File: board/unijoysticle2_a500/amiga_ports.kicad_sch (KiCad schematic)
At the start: 23 parts, among them J2 PORT JOY #1, J3 PORT JOY #2, SW3 MOUSE, SW4 SWAP, U4 74HC05, U5 74HC05, U6 74HC05

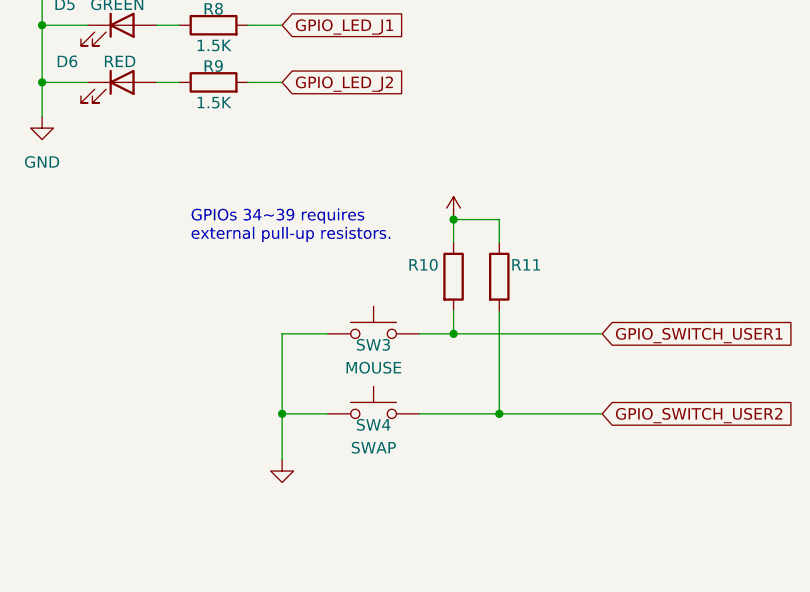
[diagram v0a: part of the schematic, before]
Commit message: a500: layout with open hardware logo in copper
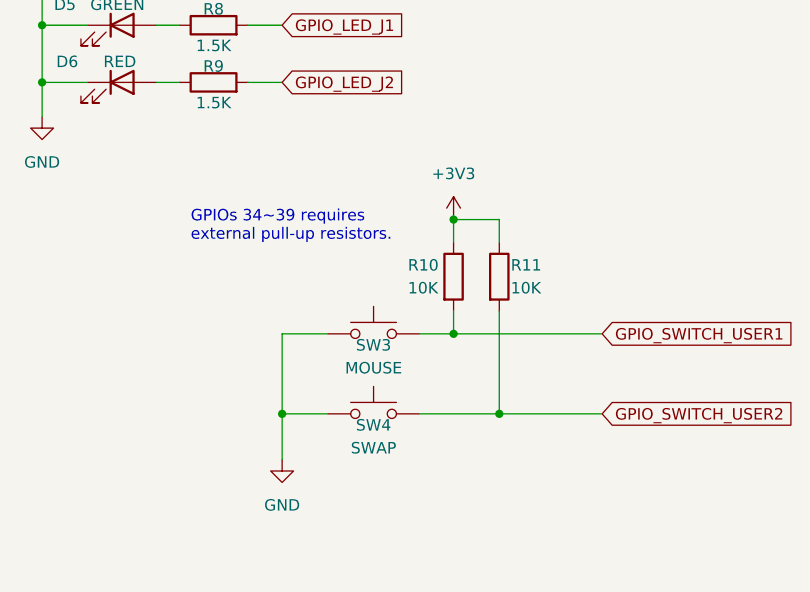
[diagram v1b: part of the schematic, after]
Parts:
- R10, R11: value (none) -> 10K; footprint (none) -> Resistor_SMD:R_0805_2012Metric_Pad1.20x1.40mm_HandSolder
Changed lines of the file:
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@@
       (effects (font (size 1.27 1.27)) (justify left))
     )
-    (property "Value" "" (id 1) (at 58.42 167.64 0)
+    (property "Value" "10K" (id 1) (at 58.42 167.64 0)
       (effects (font (size 1.27 1.27)) (justify left))
     )
-    (property "Footprint" "" (id 2) (at 61.722 166.37 90)
+    (property "Footprint" "Resistor_SMD:R_0805_2012Metric_Pad1.20x1.40mm_HandSolder" (id 2) (at 61.722 166.37 90)
       (effects (font (size 1.27 1.27)) hide)
     )
@@
       (effects (font (size 1.27 1.27)) hide)
     )
-    (property "Value" "" (id 1) (at 44.45 191.77 0))
+    (property "Value" "GND" (id 1) (at 44.45 191.77 0))
     (property "Footprint" "" (id 2) (at 44.45 186.69 0)
       (effects (font (size 1.27 1.27)) hide)
@@
       (effects (font (size 1.27 1.27)) (justify left))
     )
-    (property "Value" "" (id 1) (at 69.85 167.64 0)
+    (property "Value" "10K" (id 1) (at 69.85 167.64 0)
       (effects (font (size 1.27 1.27)) (justify left))
     )
-    (property "Footprint" "" (id 2) (at 66.802 166.37 90)
+    (property "Footprint" "Resistor_SMD:R_0805_2012Metric_Pad1.20x1.40mm_HandSolder" (id 2) (at 66.802 166.37 90)
       (effects (font (size 1.27 1.27)) hide)
     )
@@
       (effects (font (size 1.27 1.27)) hide)
     )
-    (property "Value" "" (id 1) (at 63.5 154.94 0))
+    (property "Value" "+3V3" (id 1) (at 63.5 154.94 0))
     (property "Footprint" "" (id 2) (at 63.5 160.02 0)
       (effects (font (size 1.27 1.27)) hide)

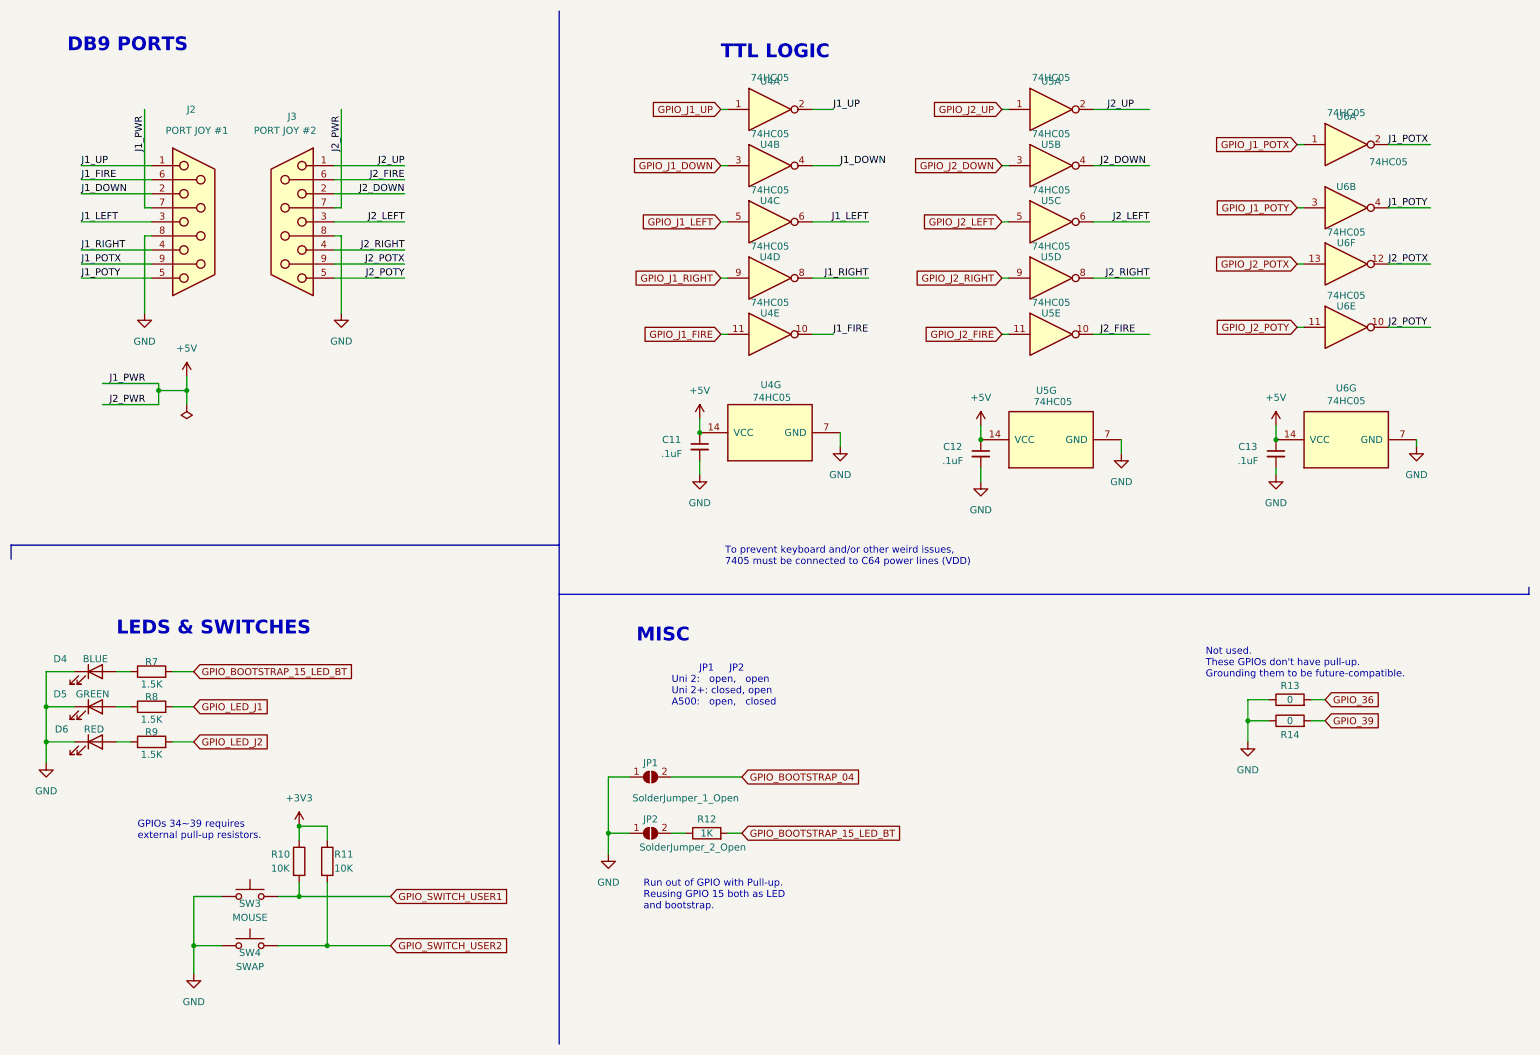
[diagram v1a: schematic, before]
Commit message: uni a500+: remove LSCS column
Values were outdated
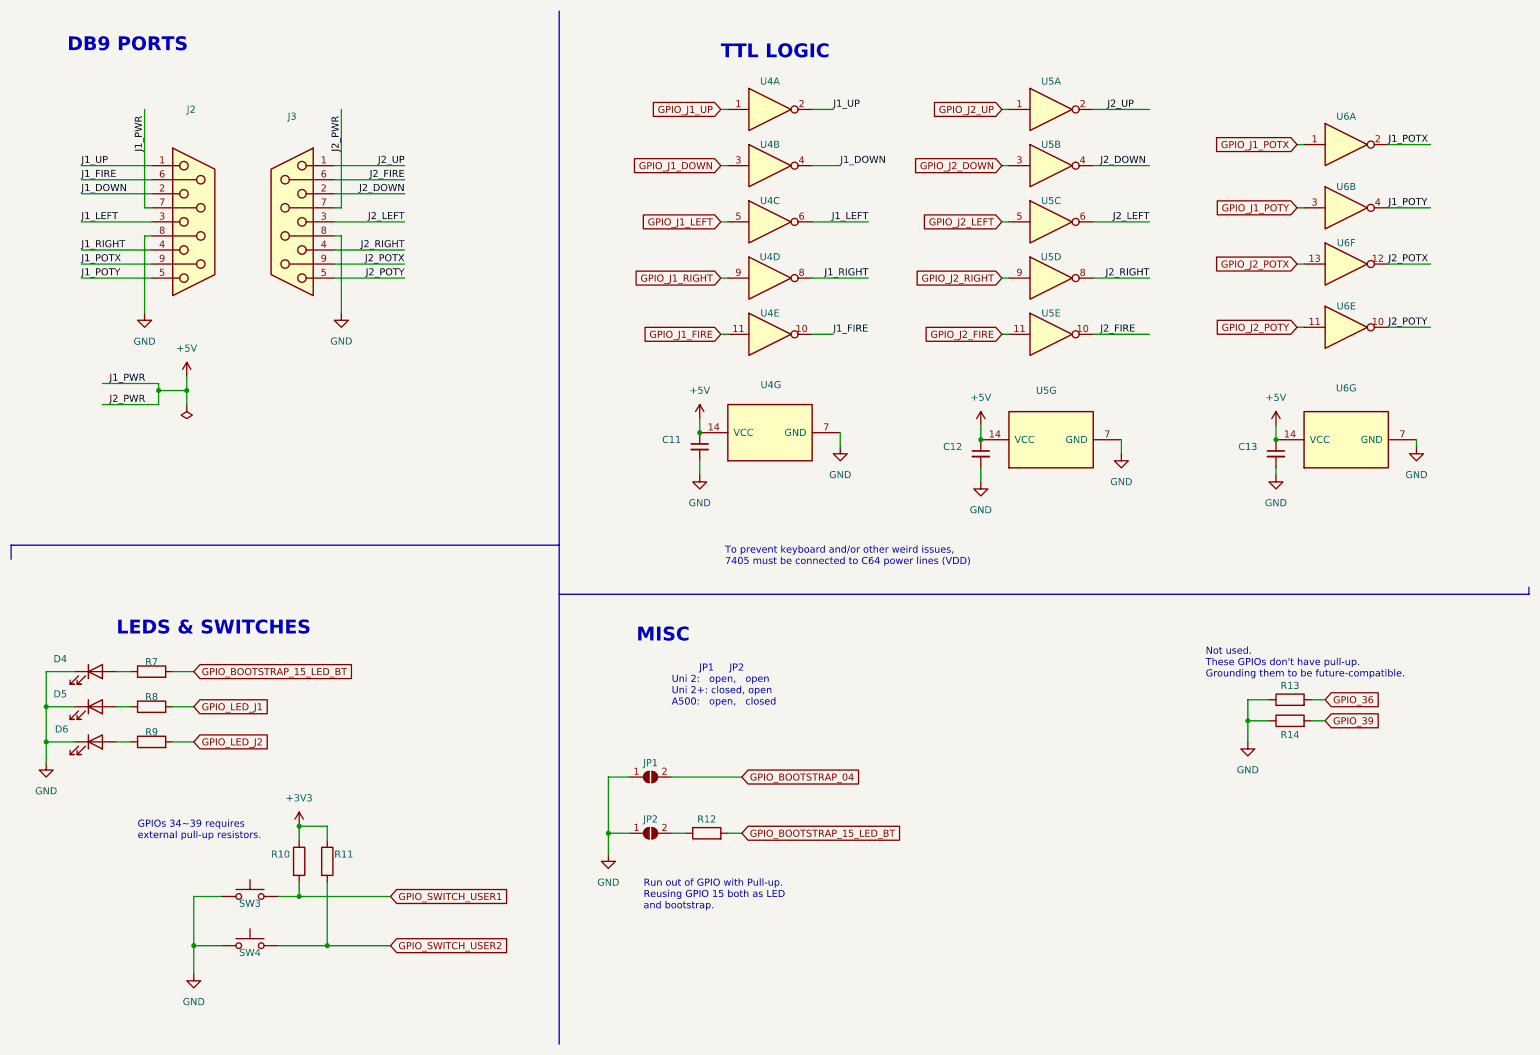
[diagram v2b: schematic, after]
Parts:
- C11, C12, C13: value .1uF -> (none); footprint Capacitor_SMD:C_0805_2012Metric_Pad1.18x1.45mm_HandSolder -> (none); LCSC C49678 -> (none)
- D4: value BLUE -> (none); footprint LED_SMD:LED_0805_2012Metric_Pad1.15x1.40mm_HandSolder -> (none); LCSC C389525 -> (none)
- D5: value GREEN -> (none); footprint LED_SMD:LED_0805_2012Metric_Pad1.15x1.40mm_HandSolder -> (none); LCSC C2297 -> (none)
- D6: value RED -> (none); footprint LED_SMD:LED_0805_2012Metric_Pad1.15x1.40mm_HandSolder -> (none); LCSC C84256 -> (none)
- J2: value PORT JOY #1 -> (none); footprint Connector_Dsub:DSUB-9_Female_Horizontal_P2.77x2.54mm_EdgePinOffset9.40mm -> (none)
- J3: value PORT JOY #2 -> (none); footprint Connector_Dsub:DSUB-9_Female_Horizontal_P2.77x2.54mm_EdgePinOffset9.40mm -> (none)
- JP1: value SolderJumper_1_Open -> (none); footprint Jumper:SolderJumper-2_P1.3mm_Open_Pad1.0x1.5mm -> (none)
- JP2: value SolderJumper_2_Open -> (none); footprint Jumper:SolderJumper-2_P1.3mm_Open_Pad1.0x1.5mm -> (none)
- R10, R11: value 10K -> (none); footprint Resistor_SMD:R_0805_2012Metric_Pad1.20x1.40mm_HandSolder -> (none)
- R12: value 1K -> (none); footprint Resistor_SMD:R_0805_2012Metric_Pad1.20x1.40mm_HandSolder -> (none)
- R13, R14: value 0 -> (none); footprint Resistor_SMD:R_0805_2012Metric_Pad1.20x1.40mm_HandSolder -> (none)
- R7, R8, R9: value 1.5K -> (none); footprint Resistor_SMD:R_0805_2012Metric_Pad1.20x1.40mm_HandSolder -> (none); LCSC C4310 -> (none)
- SW3: value MOUSE -> (none); footprint Button_Switch_THT:SW_Tactile_SPST_Angled_PTS645Vx39-2LFS -> (none)
- SW4: value SWAP -> (none); footprint Button_Switch_THT:SW_Tactile_SPST_Angled_PTS645Vx39-2LFS -> (none)
- U4, U5: value 74HC05 -> (none); footprint Package_SO:SOIC-14_3.9x8.7mm_P1.27mm -> (none); LCSC C7640 -> (none)
- U6: value 74HC05 -> (none); footprint Package_SO:SOIC-14_3.9x8.7mm_P1.27mm -> (none)

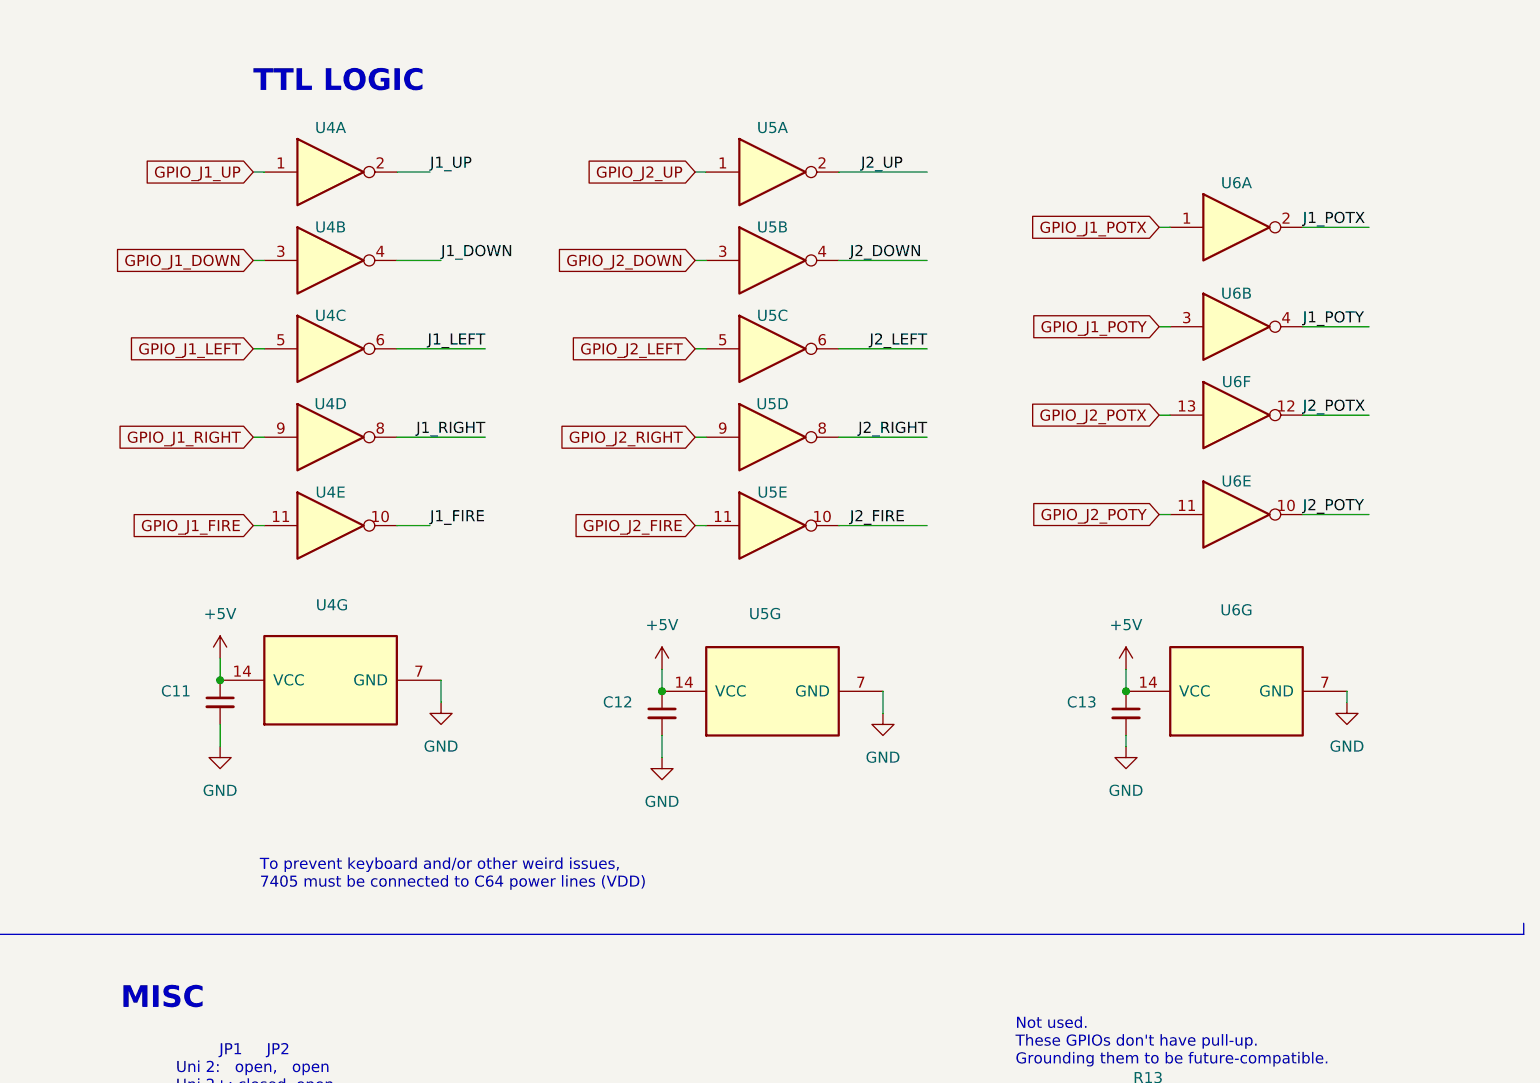
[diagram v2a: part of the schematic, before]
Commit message: uni a500: add no-connect to 74HC05 pin
In the schematic, add the no-connect to the pins that are not used.
Fixes some warnings
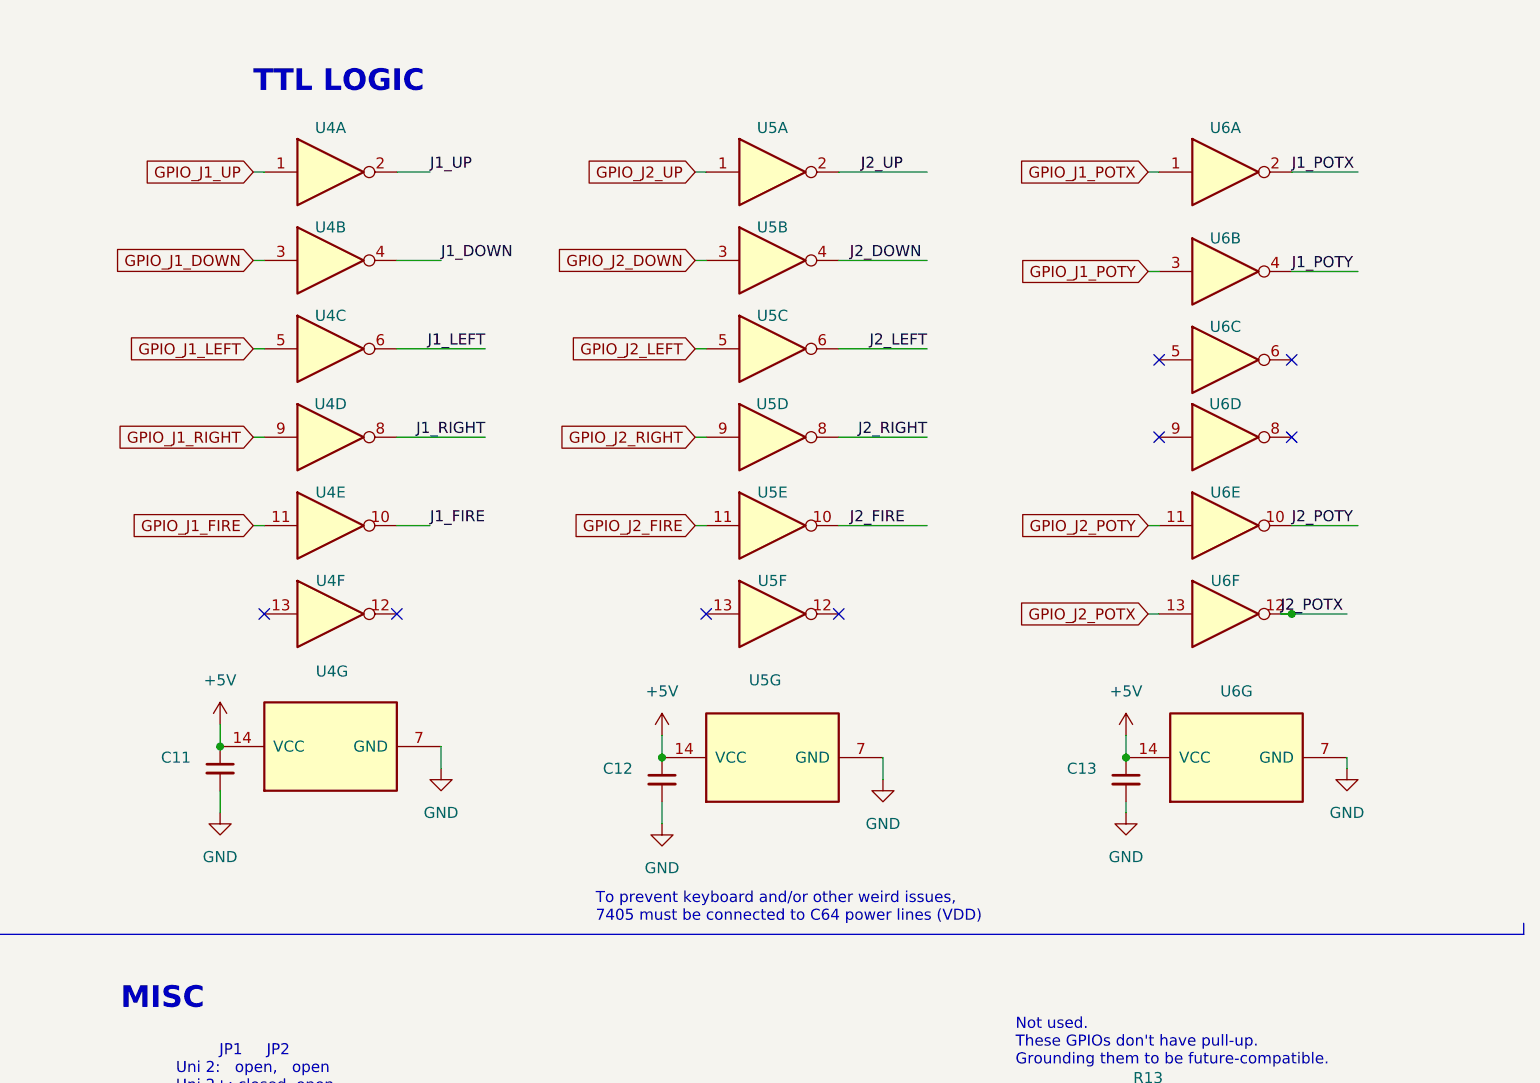
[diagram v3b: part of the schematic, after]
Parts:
- added unit 6 of U4
- added unit 6 of U5
- added unit 3 of U6
- added unit 4 of U6
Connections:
- no-connect marks 0 -> 8
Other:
- moved on the sheet: C11, C12, C13, U4G, U5G, U6A, U6B, U6E, U6F, U6G
